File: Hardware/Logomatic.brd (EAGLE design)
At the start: 61 x 38.1 mm, 71 parts, among them J1 USD_CONNECTOR, Q1 12MHz, Q2 32kHz, Q4 TRANSISTOR_PNPSMD, U1 MCP73831, U2 3.3V, U4 LPC213X, X1 USB_MICROB_PLUGCONN-11752

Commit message: Added coin cell holder
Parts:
- removed JP1: Prog, SparkFun:1X06
- removed JP2: LiPo, SparkFun:JST-2-SMD
- removed JP4: (no value), SparkFun:1X04
- removed JP5: (no value), SparkFun:1X06
- removed JP6: M100.1, SparkFun:1X10
- removed Q1: 12MHz, SparkFunEagle-6-6-07:CRYSTAL-SMD-5X3
- removed Q2: 32kHz, SparkFun:CRYSTAL-32KHZ-SMD
- removed U$1, U$2: FIDUCIAL1X2, SparkFun:FIDUCIAL-1X2
- removed U$3, U$4, U$5, U$8: STAND-OFF, SparkFun:STAND-OFF
- added BAT1: 20mm coincell, SparkFun-Electromechanical:BATTCON_20MM_4LEGS
- added D1, D2: MBRA140, SparkFun-DiscreteSemi:SMA-DIODE
- added FD1, FD2, FD3, FD4: FIDUCIAL1X2, SparkFun-Aesthetics:FIDUCIAL-1X2
- added H1, H2, H3, H4: STAND-OFF, SparkFun-Electromechanical:STAND-OFF
- added J2: ISP, SparkFun-Connectors:1X06
- added J3: LiPo, SparkFun-Connectors:JST-2-SMD
- added J4: (no value), SparkFun-Connectors:1X04
- added J5: (no value), SparkFun-Connectors:1X06
- added J6: M100.1, SparkFun-Connectors:1X10
- added Y1: 32.7680kHz, Logomatic_testing:4-SOJ_5.5MM
- added Y2: 12MHz, SparkFun-FreqCtrl:CRYSTAL-SMD-5X3
- FRAME4: value FRAME-LETTER -> FRAME-LETTERNO_PACKAGE; device SparkFun-Aesthetics:CREATIVE_COMMONS -> SparkFun-Aesthetics:DUMMY
- LED1: value LED RED -> RED
- LED3: value (none) -> RED
- Q4: value TRANSISTOR_PNPSMD -> 3906_PNP; device SparkFun:SOT23-3 -> SparkFun-DiscreteSemi:SOT23-3
- R1, R14, R6, R7: device SparkFun-Resistors:0603-RES@1 -> SparkFun-Resistors:0603-RES
- R12: value 1k -> 1K; device SparkFun-Resistors:0603-RES@1 -> SparkFun-Resistors:0603-RES
- R13, R8: value 10k -> 10K; device SparkFun-Resistors:0603-RES@1 -> SparkFun-Resistors:0603-RES
- R16, R17: value 1M -> DNP; device SparkFun-Resistors:0603-RES@1 -> SparkFun-Resistors:0603-RES
- S1: device SparkFun:AYZ0202 -> SparkFun-Electromechanical:AYZ0202
- S2: value Stop -> TAC_SWITCHSMD; device SparkFunEagle-6-6-07:TACTILE_SWITCH_SMD -> SparkFun-Retired:TACTILE-SWITCH-SMD
- S3: value Reset -> RESET; device SparkFunEagle-6-6-07:TACTILE_SWITCH_SMD -> SparkFun-Retired:TACTILE-SWITCH-SMD
- U1, U2: device SparkFun:SOT23-5 -> SparkFun-PowerIC:SOT23-5
- U4: value LPC213X -> LPC214X; device SparkFun:SQFP-S-10X10-64 -> SparkFun-DigitalIC:LQFP-10X10-64
- X1: value USB_MICROB_PLUGCONN-11752 -> (none)
- moved R18 19.9 mm to (50.0, 19.6), flipped to the bottom, turned to 180 degrees
- moved R20 16.4 mm to (55.9, 29.5), flipped to the bottom, turned to 180 degrees
- moved R19 14.3 mm to (55.9, 16.3), flipped to the bottom, turned to 180 degrees
- moved C8 2.55 mm to (26.9, 14.0)
- moved C15 2.41 mm to (26.4, 9.65), turned to 270 degrees
- moved X1 0.76 mm to (58.9, 11.3)
- moved S2 0.25 mm to (35.8, 11.4)
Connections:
- net N$16 renamed VBUS
- net N$31 renamed UP_LED
- removed net N$21: C14.2, Q1.1, U4.61
- removed net N$5: C13.2, Q1.3, U4.62
- removed net N$6: C16.2, Q2.X2, U4.3
- removed net N$9: C15.2, Q2.X1, U4.5
- removed net RST: JP1.2, R1.1, S3.3, S3.4, U4.57
- new net !RESET: J2.2, R1.1, S3.3, S3.4, U4.57
- new net N$2: BAT1.POSITIVE@1, BAT1.POSITIVE@2, BAT1.POSITIVE@3, BAT1.POSITIVE@4, D1.A
- new net RTXC1: C16.2, U4.3, Y1.1
- new net RTXC2: C15.2, U4.5, Y1.4
- new net SHIELD: X1.SHIELD1, X1.SHIELD2, X1.SHIELD3
- new net VBAT: D1.C, D2.C, U4.49
- new net XTAL1: C13.2, U4.62, Y2.3
- new net XTAL2: C14.2, U4.61, Y2.1
- net BSL: now also J2.1; no longer JP1.1
- net CS1: now also J4.1; no longer JP4.1
- net GND: now also BAT1.NEGATIVE, J2.5, J3.1, J5.4, J6.10; no longer JP1.5, JP2.1, JP5.4, JP6.10
- net MISO1: now also J4.3; no longer JP4.3
- net MOSI1: now also J4.2; no longer JP4.2
- net P1: now also J6.2; no longer JP6.2
- net P2: now also J6.3; no longer JP6.3
- net P3: now also J6.4; no longer JP6.4
- net P4: now also J6.5; no longer JP6.5
- net P5: now also J6.6; no longer JP6.6
- net P6: now also J6.7; no longer JP6.7
- net P7: now also J6.8; no longer JP6.8
- net P8: now also J6.9; no longer JP6.9
- net RAW: now also J5.1; no longer JP5.1
- net RXI-0: now also J2.4; no longer JP1.4
- net RXI-1: now also J5.6; no longer JP5.6
- net SCK1: now also J4.4; no longer JP4.4
- net STOP: now also J6.1; no longer JP6.1
- net TXO-0: now also J2.3; no longer JP1.3
- net TXO-1: now also J5.5; no longer JP5.5
- net USB_VIN: now also J5.2; no longer JP5.2
- net VCC: now also J2.6, J5.3; no longer JP1.6, JP5.3, U4.49
- net VLIPO: now also J3.2; no longer JP2.2
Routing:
- net !RESET: track 0.00 -> 41.5 mm, vias 0 -> 2
- net RST: track 41.4 -> 0.00 mm, vias 2 -> 0
- net VBAT: track 0.00 -> 17.2 mm, vias 0 -> 1
- net VCC: track 173.5 -> 186.4 mm, vias 8 -> 9
- net N$2: track 0.00 -> 11.1 mm
- net RTXC2: track 0.00 -> 10.8 mm
- net N$9: track 9.91 -> 0.00 mm
- net N$21: track 9.23 -> 0.00 mm
- net XTAL2: track 0.00 -> 8.98 mm
- net N$5: track 7.14 -> 0.00 mm
- net XTAL1: track 0.00 -> 7.04 mm
- net N$6: track 6.19 -> 0.00 mm
- net RTXC1: track 0.00 -> 5.89 mm
- net N$3: track 0.00 -> 4.46 mm, vias 0 -> 1
- net USB_VIN: track 88.3 -> 85.2 mm
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- added copper zone on layer 1, net SHIELD
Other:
- board text added: "v28"
- board text removed: "v27"

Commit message: Tweaks
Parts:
- removed LOGO3: SFE_LOGO_FLAME.4_INCH, SparkFun-Aesthetics:SFE_LOGO_FLAME_.4
- removed U$10: REVISION, SparkFun-Aesthetics:REVISION
- removed U$7: LOGO-SFESK, SparkFun:SFE-LOGO-FLAME
- added LOGO5: SFE_LOGO_FLAME.1_INCH, SparkFun-Aesthetics:SFE_LOGO_FLAME_.1
- R11: value 1.5k -> 1.5KOHM
- S1: value (none) -> BATTERY_POWER
- X1: value (none) -> Micro-B
- moved FRAME2 13.3 mm to (-0.49, -19.3)
- moved FRAME4 9.52 mm to (7.66, -19.6)
- renumbered U$6 to LOGO4
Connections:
- net GND: now also X1.GND; no longer X1.GND1
- net USB_D+: now also X1.D+; no longer X1.D+1
- net USB_D-: now also X1.D-; no longer X1.D-1
- net USB_VIN: now also X1.VBUS; no longer X1.VBUS1
- net VCC: now also D2.A
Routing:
- net VCC: track 186.4 -> 194.4 mm, vias 9 -> 10
- net N$1: track 2.05 -> 2.68 mm
- net GND: track 20.1 -> 19.9 mm, vias 27 -> 35
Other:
- board text added: "!CS"
- board text added: "0.13 Ø"
- board text added: "ALL UNITS IN INCHES"
- board text added: "Chris Taylor"
- board text added: "Revised by: Brent Wilkins & Toni Klopfenstein"
- board text removed: "C. Taylor and N. Seidle"
- board text removed: "CS"
- board text removed: "Toni Klopfenstein"

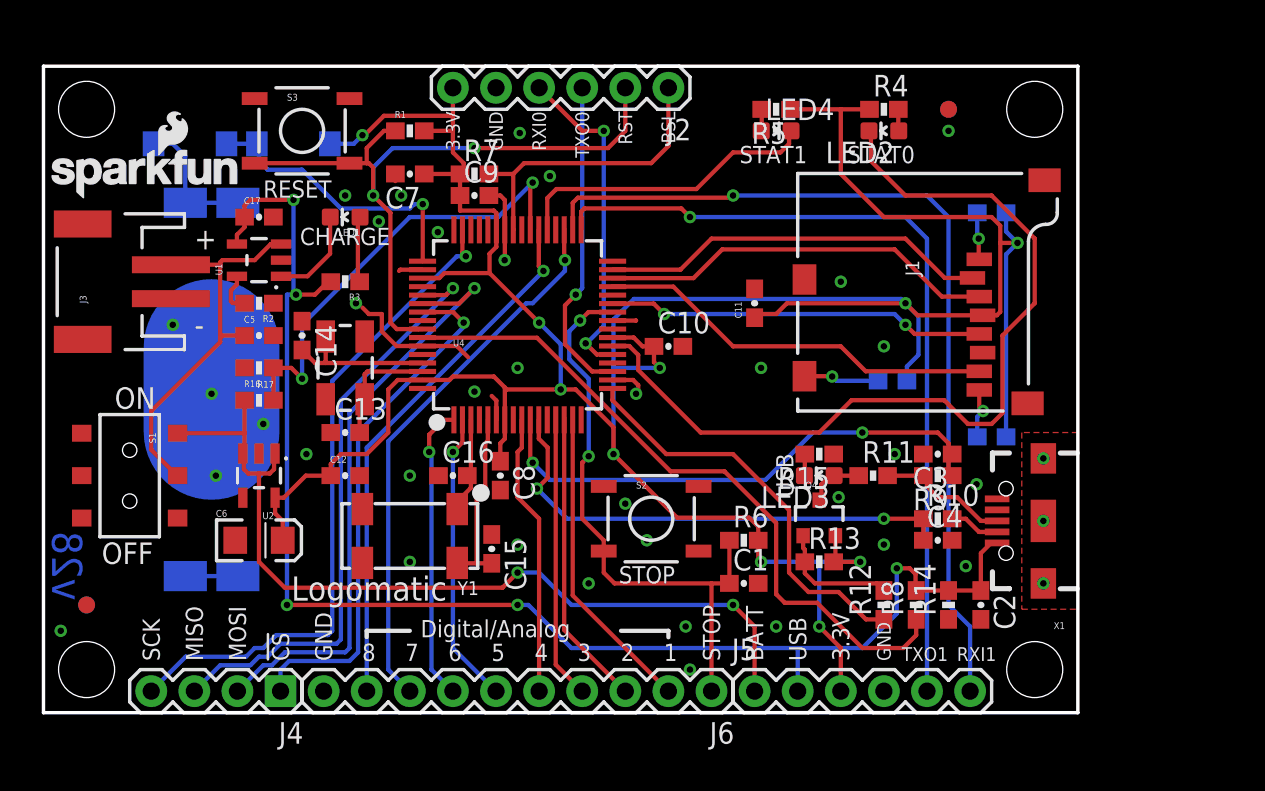
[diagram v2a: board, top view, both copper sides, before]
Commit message: Fixed issue #9 on GitHub
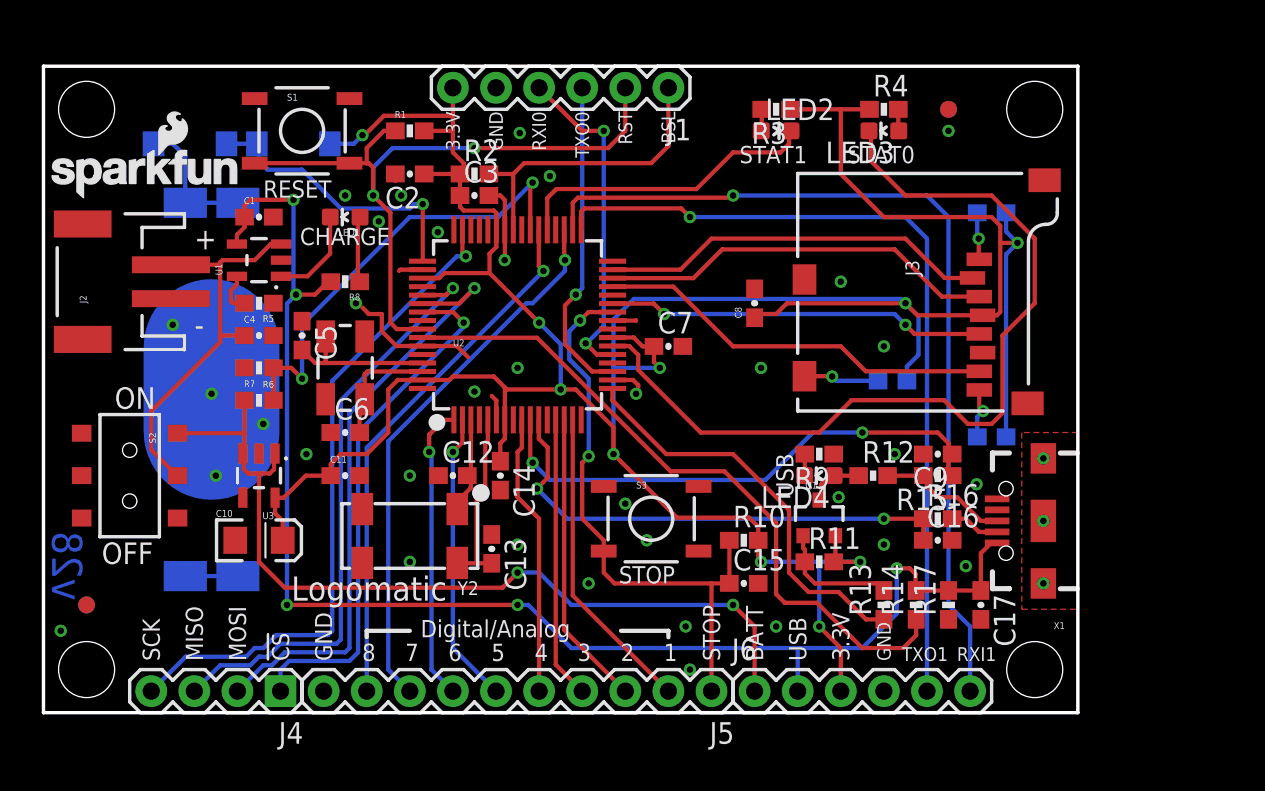
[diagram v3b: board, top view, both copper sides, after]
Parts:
- removed FRAME4: FRAME-LETTERNO_PACKAGE, SparkFun-Aesthetics:DUMMY
- removed LOGO5: SFE_LOGO_FLAME.1_INCH, SparkFun-Aesthetics:SFE_LOGO_FLAME_.1
- removed U4: LPC214X, SparkFun-DigitalIC:LQFP-10X10-64
- added FRAME1: FRAME-LETTER, SparkFun-Aesthetics:CREATIVE_COMMONS
- added LOGO100: OSHW-LOGOL, SparkFun-Aesthetics:OSHW-LOGO-L
- added U3: 3.3V, SparkFun-PowerIC:SOT23-5
- C1: value 0.1uF -> 4.7uF
- C10: value 0.1uF -> 10uF; device SparkFun-Capacitors:0603-CAP -> SparkFun-Capacitors:EIA3216
- C12: value 0.1uF -> 22pF
- C14, C15: value 22pF -> 0.1uF
- C16: value 22pF -> 18pF
- C17: value 4.7uF -> 0.1uF
- C3: value 18pF -> 0.1uF
- C4: value 18pF -> 4.7uF
- C5: value 4.7uF -> 22pF
- C6: value 10uF -> 22pF; device SparkFun-Capacitors:EIA3216 -> SparkFun-Capacitors:0603-CAP
- C9: value 0.1uF -> 18pF
- FRAME2: value FRAME-LETTER -> FRAME-LETTERNO_PACKAGE; device SparkFun-Aesthetics:CREATIVE_COMMONS -> SparkFun-Aesthetics:DUMMY
- J1: value USD_CONNECTOR -> ISP; device SparkFun-Connectors:MICRO-SD-SOCKET-PP -> SparkFun-Connectors:1X06
- J2: value ISP -> LiPo; device SparkFun-Connectors:1X06 -> SparkFun-Connectors:JST-2-SMD
- J3: value LiPo -> USD_CONNECTOR; device SparkFun-Connectors:JST-2-SMD -> SparkFun-Connectors:MICRO-SD-SOCKET-PP
- J5: value (none) -> M100.1; device SparkFun-Connectors:1X06 -> SparkFun-Connectors:1X10
- J6: value M100.1 -> (none); device SparkFun-Connectors:1X10 -> SparkFun-Connectors:1X06
- LED2: value RED -> GREEN
- LED4: value GREEN -> RED
- LOGO1: value OSHW-LOGOL -> SFE_LOGO_NAME.1_INCH; device SparkFun-Aesthetics:OSHW-LOGO-L -> SparkFun-Aesthetics:SFE_LOGO_NAME_.1
- LOGO2: value SFE_LOGO_NAME.1_INCH -> SFE_LOGO_FLAME.1_INCH; device SparkFun-Aesthetics:SFE_LOGO_NAME_.1 -> SparkFun-Aesthetics:SFE_LOGO_FLAME_.1
- R10: value 33 -> 10K
- R11: value 1.5KOHM -> 10K; device SparkFun-Resistors:0603 -> SparkFun-Resistors:0603-RES
- R12: value 1K -> 1.5KOHM; device SparkFun-Resistors:0603-RES -> SparkFun-Resistors:0603
- R13: value 10K -> 1K
- R14: value 100k -> 10K
- R15: value 330 -> 33
- R16: value DNP -> 33
- R17: value DNP -> 100k
- R2: value 2.0k -> 10K
- R5: value 330 -> 2.0k
- R6, R7: value 10K -> DNP
- R8: value 10K -> 330
- R9: value 33 -> 330
- S1: value BATTERY_POWER -> RESET; device SparkFun-Electromechanical:AYZ0202 -> SparkFun-Retired:TACTILE-SWITCH-SMD
- S2: value TAC_SWITCHSMD -> BATTERY_POWER; device SparkFun-Retired:TACTILE-SWITCH-SMD -> SparkFun-Electromechanical:AYZ0202
- S3: value RESET -> TAC_SWITCHSMD
- U2: value 3.3V -> LPC214X; device SparkFun-PowerIC:SOT23-5 -> SparkFun-DigitalIC:LQFP-10X10-64
- Y1: value 32.7680kHz -> 12MHz; device Logomatic_testing:4-SOJ_5.5MM -> SparkFun-FreqCtrl:CRYSTAL-SMD-5X3
- Y2: value 12MHz -> 32.7680kHz; device SparkFun-FreqCtrl:CRYSTAL-SMD-5X3 -> Logomatic_testing:4-SOJ_5.5MM
- moved FD1 58.6 mm to (53.3, 35.6)
- moved FD2 58.6 mm to (2.54, 6.35)
- moved H2 55.9 mm to (58.4, 35.6)
- moved H3 55.9 mm to (2.54, 2.54)
- moved C17 48.3 mm to (55.2, 6.35), turned to 270 degrees
- moved R17 43.0 mm to (53.3, 6.35), turned to 90 degrees
- moved C2 42.2 mm to (21.6, 31.8), turned to 180 degrees
- moved C4 41.8 mm to (12.7, 22.2)
- moved J3 41.3 mm to (44.5, 17.8), turned to 270 degrees
- moved R16 40.6 mm to (52.7, 11.4)
- moved R8 38.7 mm to (17.8, 25.4), turned to 180 degrees
- moved C1 35.8 mm to (12.7, 29.2)
- moved J2 34.9 mm to (3.81, 25.4), turned to 90 degrees
- moved H1 33.0 mm to (2.54, 35.6)
- moved H4 33.0 mm to (58.4, 2.54)
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- renumbered BAT1 to BAT100, D1 to D101, D2 to D100, FD3 to FD100, FD4 to FD101, LOGO4 to LOGO101, Q4 to Q1, R18 to R101, R19 to R100, R20 to R102
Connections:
- net !CS0: now also J3.CS, U2.31; no longer J1.CS, U4.31
- net !RESET: now also J1.2, S1.3, S1.4, U2.57; no longer J2.2, S3.3, S3.4, U4.57
- net BATTLVL: now also R6.1, R7.2, U2.39; no longer R16.2, R17.1, U4.39
- net BSL: now also J1.1, R2.2, U2.41; no longer J2.1, R7.2, U4.41
- net CD: now also J3.CD2; no longer J1.CD2
- net CS1: now also U2.55; no longer U4.55
- net GND: now also C10.C, C12.1, C14.2, C15.2, C16.2, C5.1, C6.1, J1.5, J2.1, J3.GND, J3.GND1, J3.GND3, J5.10, J6.4, R17.1, R5.1, R6.2, R9.1, S1.1, S1.2, U2.18, U2.25, U2.42, U2.50, U2.59, U2.6, U3.2; no longer C10.2, C12.2, C14.1, C15.1, C16.1, C5.2, C6.C, J1.GND, J1.GND1, J1.GND3, J2.5, J3.1, J5.4, J6.10, R14.1, R15.1, R17.2, R2.1, S2.1, S3.2, U2.2, U4.18, U4.25, U4.42, U4.50, U4.59, U4.6
- net MISO0: now also J3.DO, U2.29; no longer J1.DO, U4.29
- net MISO1: now also U2.53; no longer U4.53
- net MOSI0: now also J3.DI, U2.30; no longer J1.DI, U4.30
- net MOSI1: now also U2.54; no longer U4.54
- net N$1: now also R5.2; no longer R2.2
- net N$10: now also J3.RSV2; no longer J1.RSV2
- net N$13: now also R8.1; no longer R3.1
- net N$17: now also R11.1, R13.2; no longer R12.2, R13.1
- net N$19: now also LED2.A, R3.2; no longer LED4.A, R5.2
- net N$3: now also J3.CD1; no longer J1.CD1
- net N$33: now also LED4.C, R9.2; no longer LED3.C, R15.2
- net N$4: now also J3.RSV1; no longer J1.RSV1
- net N$7: now also LED3.A; no longer LED2.A
- net P-D+: now also C9.1, R15.1, U2.10; no longer C3.1, R9.1, U4.10
- net P-D-: now also C16.1, R16.1, U2.11; no longer C4.1, R10.1, U4.11
- net P1: now also J5.2, U2.15; no longer J6.2, U4.15
- net P2: now also J5.3, U2.14; no longer J6.3, U4.14
- net P3: now also J5.4, U2.13; no longer J6.4, U4.13
- net P4: now also J5.5, U2.9; no longer J6.5, U4.9
- net P5: now also J5.6, U2.2; no longer J6.6, U4.2
- net P6: now also J5.7, U2.1; no longer J6.7, U4.1
- net P7: now also J5.8, U2.35; no longer J6.8, U4.35
- net P8: now also J5.9, U2.38; no longer J6.9, U4.38
- net RAW: now also J6.1, R7.1, S2.1, U3.1, U3.3; no longer J5.1, R16.1, S1.1, U2.1, U2.3
- net RTXC1: now also C12.2, U2.3, Y2.1; no longer C16.2, U4.3, Y1.1
- net RTXC2: now also C13.2, U2.5, Y2.4; no longer C15.2, U4.5, Y1.4
- net RXI-0: now also J1.4, U2.21; no longer J2.4, U4.21
- net RXI-1: now also J6.6, U2.34; no longer J5.6, U4.34
- net SCK0: now also J3.SCLK, U2.27; no longer J1.SCLK, U4.27
- net SCK1: now also U2.47; no longer U4.47
- net STAT: now also LED4.A, R12.1; no longer LED3.A, R11.1
- net STAT0: now also LED3.C, U2.22; no longer LED2.C, U4.22
- net STAT1: now also LED2.C, U2.37; no longer LED4.C, U4.37
- net STOP: now also C15.1, J5.1, R10.1, S3.3, U2.26; no longer C1.1, J6.1, R6.1, S2.3, U4.26
- net TXO-0: now also J1.3, U2.19; no longer J2.3, U4.19
- net TXO-1: now also J6.5, U2.33; no longer J5.5, U4.33
- net UP_LED: now also R13.1, U2.17; no longer R12.1, U4.17
- net USB_D+: now also R12.2, R15.2; no longer R11.2, R9.2
- net USB_D-: now also R16.2; no longer R10.2
- net USB_VIN: now also C1.1, J6.2, R17.2; no longer C2.1, J5.2, R3.2
- net VBAT: now also U2.49; no longer U4.49
- net VBUS: now also R14.1, U2.58; no longer R8.1, U4.58
- net VCC: now also C10.A, C14.1, C2.1, C3.1, J1.6, J3.VCC, J6.3, R10.2, R11.2, R2.1, R3.1, U2.23, U2.43, U2.51, U2.63, U2.7, U3.5; no longer C10.1, C12.1, C6.A, C9.1, J1.VCC, J2.6, J5.3, R13.2, R5.1, R6.2, R7.1, U2.5, U4.23, U4.43, U4.51, U4.63, U4.7
- net VLIPO: now also C4.1, J2.2, S2.2; no longer C5.1, J3.2, S1.2
- net XTAL1: now also C6.2, U2.62, Y1.3; no longer C13.2, U4.62, Y2.3
- net XTAL2: now also C5.2, U2.61, Y1.1; no longer C14.2, U4.61, Y2.1
